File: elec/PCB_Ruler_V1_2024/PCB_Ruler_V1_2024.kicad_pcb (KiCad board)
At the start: 2 copper layers, 155 x 30 mm, 51 parts, among them J1 USB-C, J2 S2B-XH-A-1LFSN, SW1 CS1213AGF260, SW2 CS1213AGF260, SW3 CS1213AGF260, SW4 CS1213AGF260, SW5 CS1213AGF260, SW6 CS1213AGF260, SW7 CS1213AGF260, U1 ESP32-C3-WROOM-02-H4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

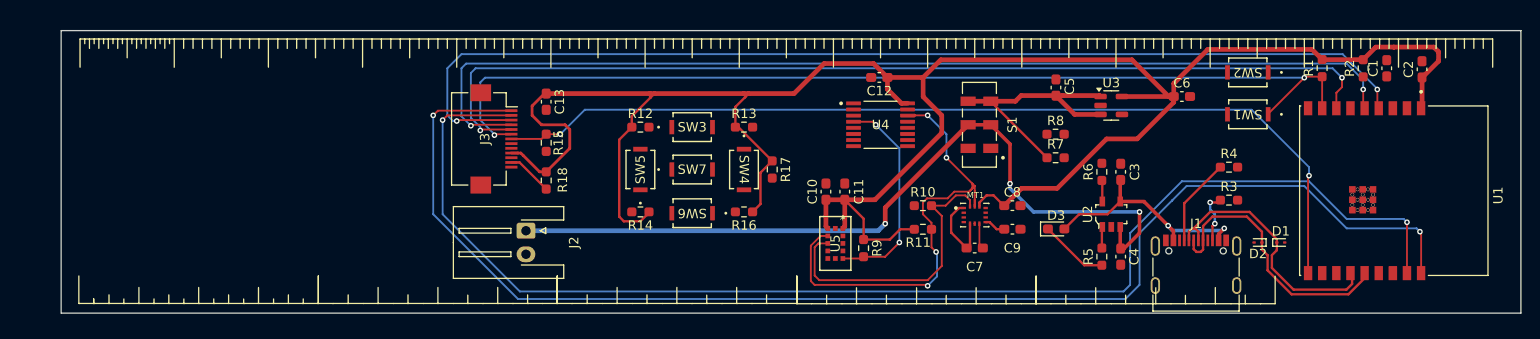
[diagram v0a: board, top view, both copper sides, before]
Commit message: Added to schematic what was missing
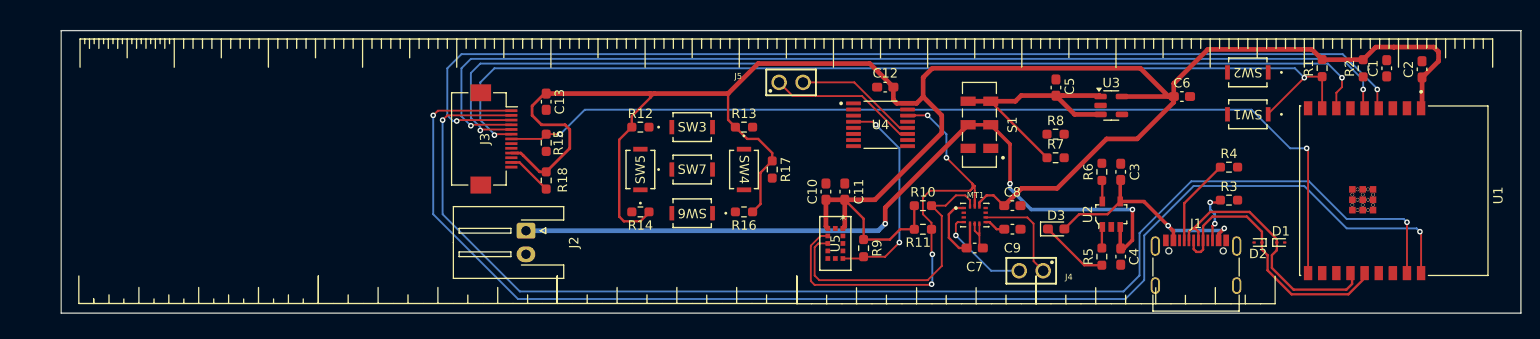
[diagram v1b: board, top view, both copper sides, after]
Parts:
- added J4: 61300211121, Header2_1:61300211121, F.Cu at (201.5, 148.0)
- added J5: 61300211121, Header2_1:61300211121, F.Cu at (176.0, 128.0)
- moved C12 1.20 mm to (186.0, 128.5)
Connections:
- MT1 pad 4: INT1_IMU -> INT1_IMU/RX
- MT1 pad 9: INT2_IMU -> INT2_IMU/TX
- U1 pad 11: unconnected-(U1-RXD-Pad11) -> INT1_IMU/RX
- U1 pad 12: unconnected-(U1-TXD-Pad12) -> INT2_IMU/TX
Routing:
- net IO7: track 0.00 -> 15.9 mm
- net IO8: track 0.00 -> 13.1 mm
- net INT2_IMU/TX: track 0.00 -> 10.8 mm
- net INT1_IMU/RX: track 0.00 -> 10.4 mm, vias 0 -> 1
- net GND: track 2.81 -> 4.27 mm
- net CS_Ecran: track 99.8 -> 100.7 mm
- net Vbat+: track 84.6 -> 83.7 mm
- net RESET_Ecran: track 106.9 -> 107.7 mm
- net AVDD: track 249.5 -> 250.1 mm
- net Touch1: track 138.6 -> 138.0 mm
- net Touch0: track 142.2 -> 141.7 mm

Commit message: hi sexy ;)
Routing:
- net SDA: track 31.2 -> 107.5 mm, vias 0 -> 3
- net SCL: track 50.1 -> 117.2 mm, vias 4 -> 5
- net INT_IO_Extender: track 0.00 -> 57.7 mm, vias 0 -> 2
- net INT1_IMU/RX: track 10.4 -> 60.0 mm, vias 1 -> 2
- net INT2_IMU/TX: track 10.8 -> 59.6 mm, vias 0 -> 1
- net Val_Bat: track 0.00 -> 42.6 mm, vias 0 -> 2
- net Button5: track 0.00 -> 33.4 mm
- net Button3: track 0.00 -> 28.5 mm, vias 0 -> 2
- net Button4: track 0.00 -> 26.7 mm
- net AVDD: track 250.1 -> 275.2 mm, vias 0 -> 2
- net Button1: track 0.00 -> 25.0 mm, vias 0 -> 2
- net EN: track 0.00 -> 17.4 mm
- net Button2: track 0.00 -> 14.1 mm
- net CS_Ecran: track 100.7 -> 102.6 mm
- net Touch1: track 138.0 -> 136.1 mm
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
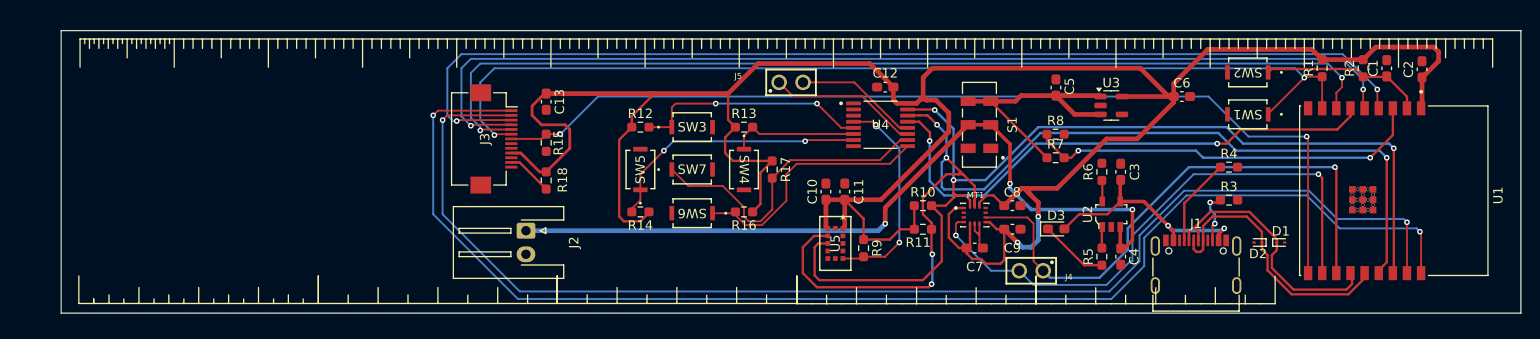
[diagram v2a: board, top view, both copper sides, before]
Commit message: PCB no errors
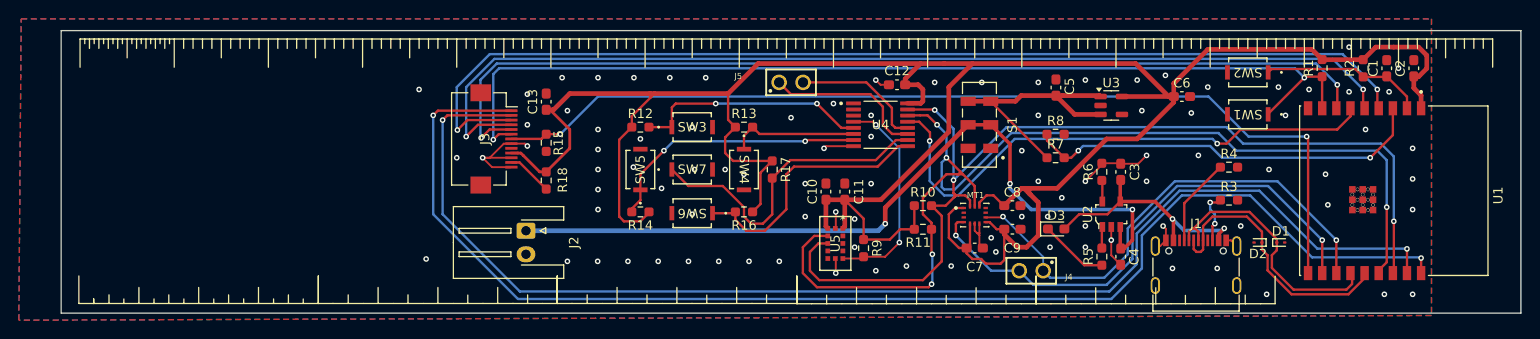
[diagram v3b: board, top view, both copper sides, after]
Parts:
- moved C12 1.27 mm to (187.2, 128.2)
- moved C2 0.88 mm to (242.1, 126.5)
- turned C13 to 90 degrees
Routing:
- net GND: track 4.52 -> 41.4 mm, vias 0 -> 96
- net INT2_IMU/TX: track 59.6 -> 52.8 mm, vias 1 -> 2
- net INT1_IMU/RX: track 60.0 -> 55.2 mm
- net RS: track 106.9 -> 105.0 mm
- net SPI_MOSI: track 115.2 -> 113.6 mm
- net Touch1: track 136.1 -> 134.8 mm
- net Button4: track 26.7 -> 28.0 mm
- net Touch0: track 139.9 -> 138.6 mm
- net IO7: track 15.9 -> 17.0 mm
- net SCL: track 117.2 -> 116.1 mm
- net IO8: track 13.1 -> 14.1 mm
- net RESET_Ecran: track 107.7 -> 107.0 mm
- net SPI_CLK: track 111.1 -> 110.5 mm
- net Button5: track 33.4 -> 33.9 mm
- net AVDD: track 275.2 -> 275.7 mm, vias 2 -> 0
- added copper zone on B.Cu, net GND
- added copper zone on F.Cu, net GND

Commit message: last push before order
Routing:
- net GND: track 41.4 -> 48.4 mm, vias 96 -> 95
- net SCL: track 116.1 -> 115.2 mm
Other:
- board text added: "+"
- board text added: "-"
- board text added: "0"
- board text added: "1"
- board text added: "10"
- board text added: "11"
- board text added: "12"
- board text added: "13"
- board text added: "14"
- board text added: "15"
- board text added: "2"
- board text added: "3"
- board text added: "4"
- board text added: "5"
- board text added: "6"
- board text added: "7"
- board text added: "8"
- board text added: "9"
- board text added: "A24_Ruler"
- board text added: "Francis Gratton Laurie-Anne Boudreault"
- board text added: "IO7"
- board text added: "IO8"
- board text added: "RX"
- board text added: "TX"
